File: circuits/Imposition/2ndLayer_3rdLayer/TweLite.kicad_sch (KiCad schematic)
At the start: 14 parts, among them SW3 SW_SPST, SW4 SW_SPST, U2 TWE-L-WX

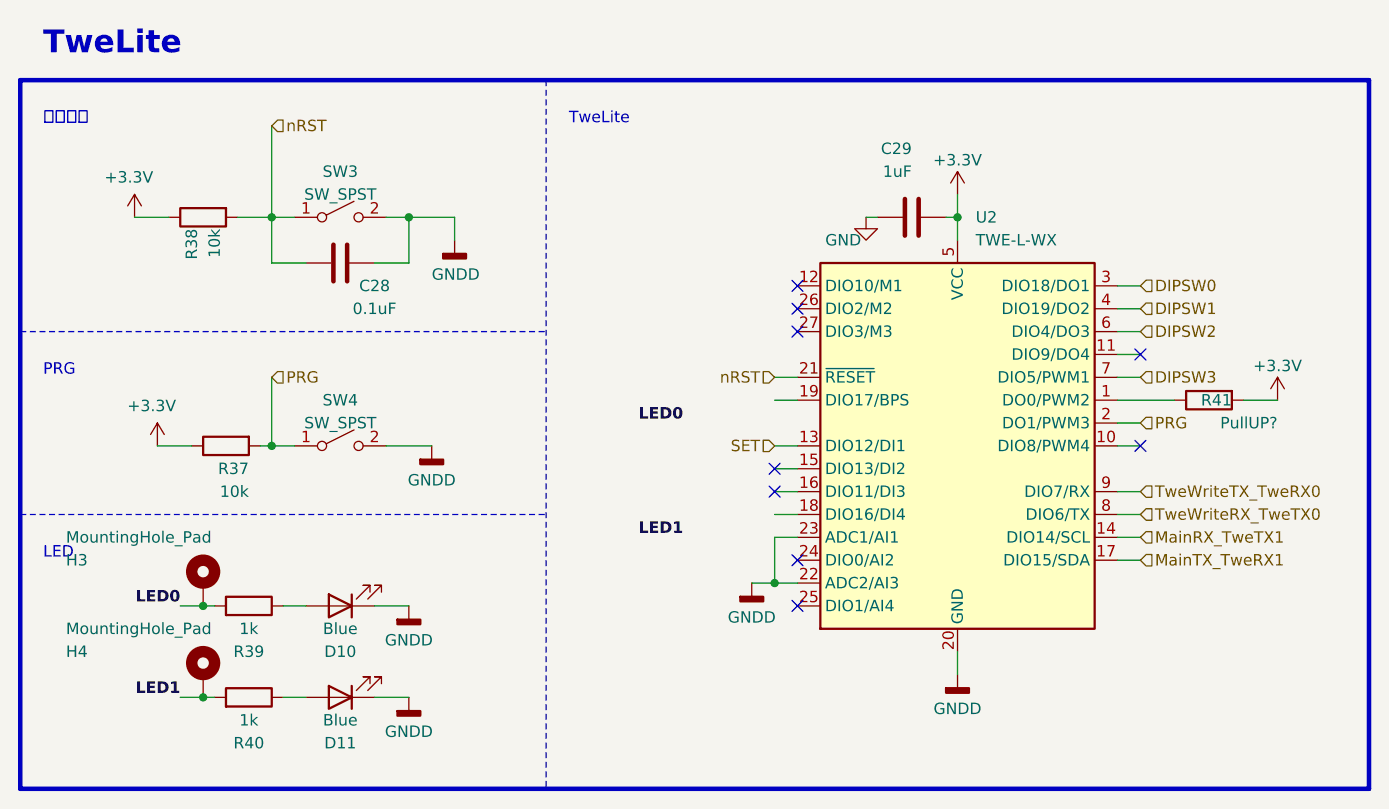
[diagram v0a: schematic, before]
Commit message: 発注_第一弾
Drive, 1stLayer_Power, 2ndLayer_3rdLayer
を発注
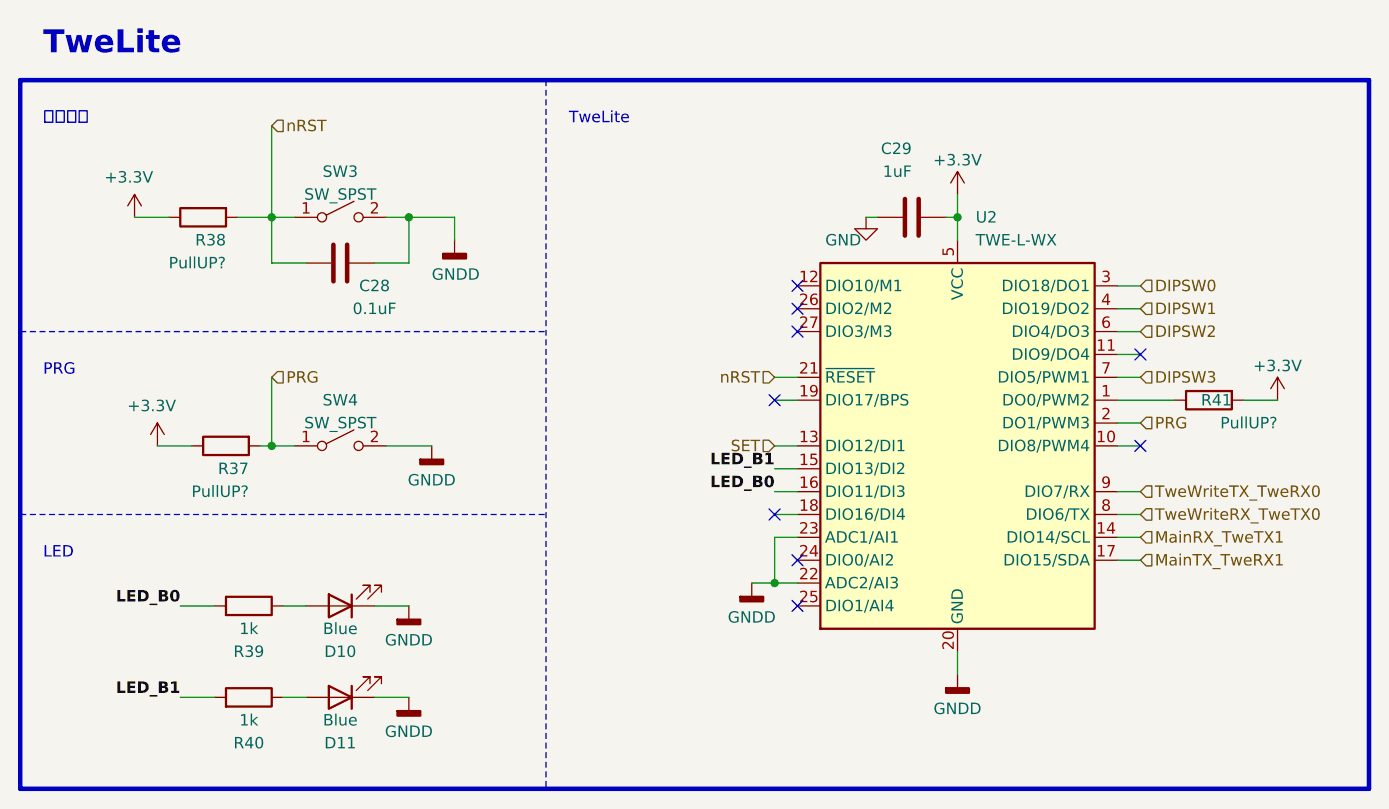
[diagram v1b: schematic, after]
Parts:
- removed H3, H4: MountingHole_Pad, TestPoint:TestPoint_Pad_1.0x1.0mm, symbol Mechanical:MountingHole_Pad
- R37, R38: value 10k -> PullUP?
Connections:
- net LED0 is gone; now on net LED_B0: R39.2
- net LED1 is gone; now on net LED_B1: R40.2
- net LED_B1: now reaches U2.15 (DIO13/DI2)
- net LED_B0: now reaches U2.16 (DIO11/DI3)
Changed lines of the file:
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@@
   (junction (at 170.18 73.66) (diameter 0) (color 0 0 0 0)
   )
-  (junction (at 86.36 116.84) (diameter 0) (color 0 0 0 0)
-  )
   (junction (at 93.98 73.66) (diameter 0) (color 0 0 0 0)
   )
@@
   (junction (at 109.22 73.66) (diameter 0) (color 0 0 0 0)
   )
-  (junction (at 86.36 127) (diameter 0) (color 0 0 0 0)
-  )
   (no_connect (at 152.4 86.36))
-  (no_connect (at 149.86 101.6))
+  (no_connect (at 149.86 106.68))
   (no_connect (at 190.5 99.06))
-  (no_connect (at 149.86 104.14))
   (no_connect (at 152.4 111.76))
   (no_connect (at 152.4 81.28))
+  (no_connect (at 149.86 93.98))
   (no_connect (at 152.4 116.84))
   (no_connect (at 152.4 83.82))
@@
     (stroke (width 0) (type default))
   )
-  (wire (pts (xy 86.36 116.84) (xy 87.63 116.84))
-    (stroke (width 0) (type default))
-  )
   (wire (pts (xy 149.86 109.22) (xy 149.86 114.3))
     (stroke (width 0) (type default))
@@
     (stroke (width 0) (type default))
   )
-  (wire (pts (xy 83.82 116.84) (xy 86.36 116.84))
+  (wire (pts (xy 83.82 116.84) (xy 87.63 116.84))
     (stroke (width 0) (type default))
   )
@@
     (stroke (width 0) (type default))
   )
+  (wire (pts (xy 149.86 101.6) (xy 152.4 101.6))
+    (stroke (width 0) (type default))
+  )
   (wire (pts (xy 170.18 73.66) (xy 170.18 76.2))
     (stroke (width 0) (type default))
@@
     (stroke (width 0) (type default))
   )
-  (wire (pts (xy 83.82 127) (xy 86.36 127))
+  (wire (pts (xy 83.82 127) (xy 87.63 127))
     (stroke (width 0) (type default))
   )
@@
     (stroke (width 0) (type default))
   )
-  (wire (pts (xy 149.86 101.6) (xy 152.4 101.6))
-    (stroke (width 0) (type default))
-  )
   (wire (pts (xy 114.3 73.66) (xy 114.3 76.2))
-    (stroke (width 0) (type default))
-  )
-  (wire (pts (xy 86.36 127) (xy 87.63 127))
     (stroke (width 0) (type default))
   )
@@
     (effects (font (size 2.54 2.54) (thickness 0.508) bold) (justify left bottom))
   )
-  (label "LED0" (at 139.7 96.52 180) (fields_autoplaced)
+  (label "LED_B0" (at 149.86 104.14 180) (fields_autoplaced)
     (effects (font (size 1.27 1.27) (thickness 0.254) bold) (justify right bottom))
   )
-  (label "LED1" (at 83.82 127 180) (fields_autoplaced)
+  (label "LED_B1" (at 83.82 127 180) (fields_autoplaced)
     (effects (font (size 1.27 1.27) (thickness 0.254) bold) (justify right bottom))
   )
-  (label "LED1" (at 139.7 109.22 180) (fields_autoplaced)
+  (label "LED_B1" (at 149.86 101.6 180) (fields_autoplaced)
     (effects (font (size 1.27 1.27) (thickness 0.254) bold) (justify right bottom))
   )
-  (label "LED0" (at 83.82 116.84 180) (fields_autoplaced)
+  (label "LED_B0" (at 83.82 116.84 180) (fields_autoplaced)
     (effects (font (size 1.27 1.27) (thickness 0.254) bold) (justify right bottom))
   )
@@
       (effects (font (size 1.27 1.27)) (justify left))
     )
-    (property "Value" "10k" (at 91.44 104.14 90)
+    (property "Value" "PullUP?" (at 91.44 104.14 90)
       (effects (font (size 1.27 1.27)) (justify left))
     )
@@
   (symbol (lib_id "Device:R") (at 86.36 73.66 90) (mirror x) (unit 1)
     (in_bom yes) (on_board yes) (dnp no)
-    (property "Reference" "R38" (at 85.09 74.93 0)
-      (effects (font (size 1.27 1.27)) (justify left))
-    )
-    (property "Value" "10k" (at 87.63 74.93 0)
+    (property "Reference" "R38" (at 88.9 76.2 90)
+      (effects (font (size 1.27 1.27)) (justify left))
+    )
+    (property "Value" "PullUP?" (at 88.9 78.74 90)
       (effects (font (size 1.27 1.27)) (justify left))
     )
@@
         )
       )
-    )
-  )
-  (symbol (lib_id "Mechanical:MountingHole_Pad") (at 86.36 114.3 0) (mirror y) (unit 1)
-    (in_bom yes) (on_board yes) (dnp no)
-    (property "Reference" "H3" (at 71.12 111.76 0)
-      (effects (font (size 1.27 1.27)) (justify right))
-    )
-    (property "Value" "MountingHole_Pad" (at 71.12 109.22 0)
-      (effects (font (size 1.27 1.27)) (justify right))
-    )
-    (property "Footprint" "TestPoint:TestPoint_Pad_1.0x1.0mm" (at 86.36 114.3 0)
-      (effects (font (size 1.27 1.27)) hide)
-    )
-    (property "Datasheet" "~" (at 86.36 114.3 0)
-      (effects (font (size 1.27 1.27)) hide)
-    )
-    (pin "1")
-    (instances
-      (project "2ndLayer_3rdLayer"
-        (path "/5cc21ad3-a17c-4615-8f1b-99935a785699/682cbe04-57d1-42aa-ad60-367d6b4ba6c6/cf126de1-9acf-4e9a-958a-0e6f99db88bb"
-          (reference "H3") (unit 1)
-        )
-      )
-    )
-  )
-  (symbol (lib_id "Mechanical:MountingHole_Pad") (at 86.36 124.46 0) (mirror y) (unit 1)
-    (in_bom yes) (on_board yes) (dnp no)
-    (property "Reference" "H4" (at 71.12 121.92 0)
-      (effects (font (size 1.27 1.27)) (justify right))
-    )
-    (property "Value" "MountingHole_Pad" (at 71.12 119.38 0)
-      (effects (font (size 1.27 1.27)) (justify right))
-    )
-    (property "Footprint" "TestPoint:TestPoint_Pad_1.0x1.0mm" (at 86.36 124.46 0)
-      (effects (font (size 1.27 1.27)) hide)
-    )
-    (property "Datasheet" "~" (at 86.36 124.46 0)
-      (effects (font (size 1.27 1.27)) hide)
-    )
-    (pin "1")
-    (instances
-      (project "2ndLayer_3rdLayer"
-        (path "/5cc21ad3-a17c-4615-8f1b-99935a785699/682cbe04-57d1-42aa-ad60-367d6b4ba6c6/cf126de1-9acf-4e9a-958a-0e6f99db88bb"
-          (reference "H4") (unit 1)
-        )
-      )
